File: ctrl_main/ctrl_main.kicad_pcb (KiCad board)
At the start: 2 copper layers, 53.3 x 101.6 mm, 18 parts, among them IC1 SN74HC125N, J1 B2B-XH-A(LF)(SN), J2 B2B-XH-A(LF)(SN), J3 B2B-XH-A(LF)(SN), P1 ANALOG, P2 DIGITAL_L, P3 DIGITAL_H, P4 JS_H, P5 JS_V, P6 SDC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

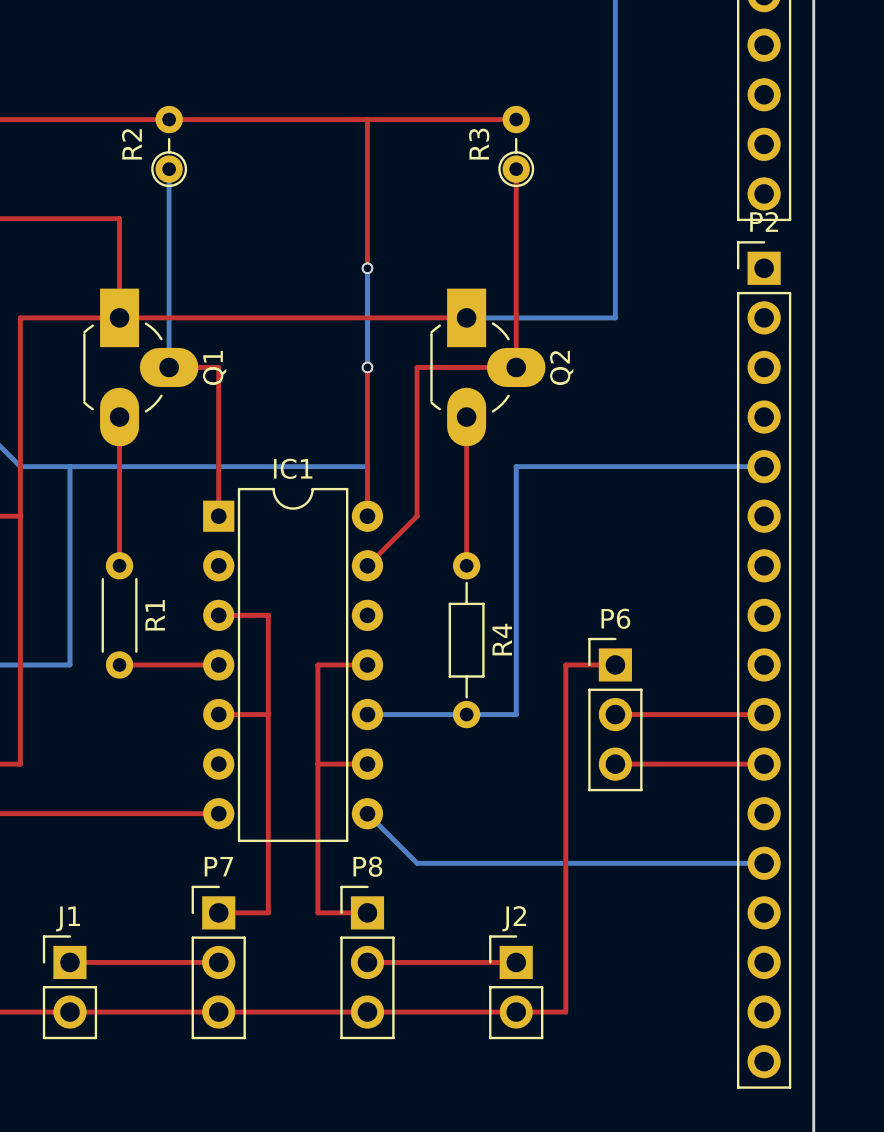
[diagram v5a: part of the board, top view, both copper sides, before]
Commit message: mod ctrl_main wiring
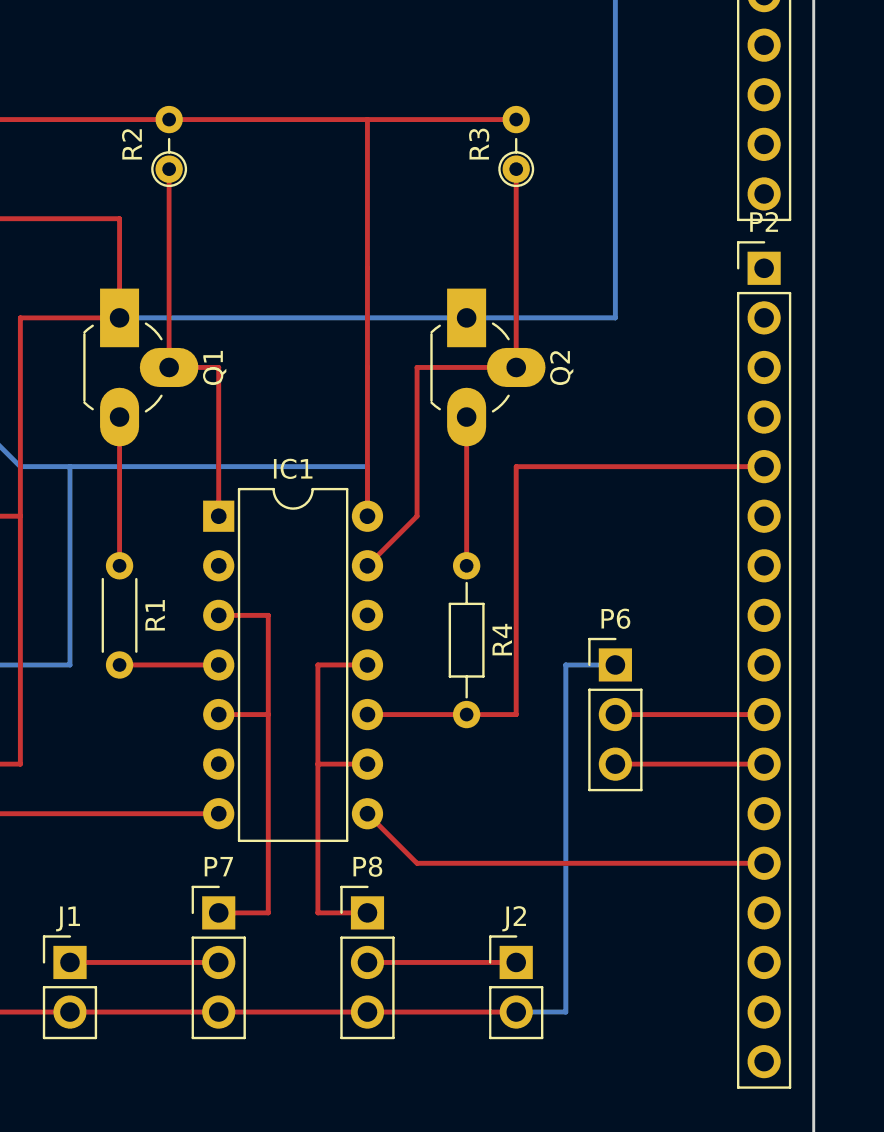
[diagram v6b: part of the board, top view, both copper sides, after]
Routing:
- net 5V: vias 2 -> 0
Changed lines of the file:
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@@
     (thickness 1.6)
     (drawings 23)
-    (tracks 81)
+    (tracks 79)
     (zones 0)
     (modules 18)
@@
   )
   (segment (start 214.63 124.46) (end 222.25 124.46) (width 0.25) (layer F.Cu) (net 1))
-  (segment (start 237.49 127) (end 240.03 127) (width 0.25) (layer F.Cu) (net 2))
-  (segment (start 240.03 109.22) (end 242.57 109.22) (width 0.25) (layer F.Cu) (net 2))
-  (segment (start 240.03 127) (end 240.03 109.22) (width 0.25) (layer F.Cu) (net 2))
+  (segment (start 217.17 91.44) (end 234.95 91.44) (width 0.25) (layer B.Cu) (net 2))
+  (segment (start 242.57 109.22) (end 240.03 109.22) (width 0.25) (layer B.Cu) (net 2))
+  (segment (start 240.03 127) (end 237.49 127) (width 0.25) (layer B.Cu) (net 2))
+  (segment (start 240.03 109.22) (end 240.03 127) (width 0.25) (layer B.Cu) (net 2))
   (segment (start 212.09 101.6) (end 212.09 91.44) (width 0.25) (layer F.Cu) (net 2))
   (segment (start 212.09 91.44) (end 217.17 91.44) (width 0.25) (layer F.Cu) (net 2))
@@
   (segment (start 212.09 101.6) (end 212.09 114.3) (width 0.25) (layer F.Cu) (net 2))
   (segment (start 234.95 91.44) (end 242.57 91.44) (width 0.25) (layer B.Cu) (net 2))
+  (segment (start 242.57 91.44) (end 242.57 71.12) (width 0.25) (layer B.Cu) (net 2))
+  (segment (start 242.57 71.12) (end 243.84 69.85) (width 0.25) (layer B.Cu) (net 2))
   (segment (start 243.84 69.85) (end 250.19 69.85) (width 0.25) (layer B.Cu) (net 2))
-  (segment (start 242.57 71.12) (end 243.84 69.85) (width 0.25) (layer B.Cu) (net 2))
-  (segment (start 242.57 91.44) (end 242.57 71.12) (width 0.25) (layer B.Cu) (net 2))
-  (segment (start 217.17 91.44) (end 234.95 91.44) (width 0.25) (layer F.Cu) (net 2))
   (segment (start 217.17 91.44) (end 217.17 86.36) (width 0.25) (layer F.Cu) (net 2))
   (segment (start 217.17 86.36) (end 209.55 86.36) (width 0.25) (layer F.Cu) (net 2))
@@
   (segment (start 201.93 86.36) (end 201.93 83.82) (width 0.25) (layer B.Cu) (net 2))
   (segment (start 229.87 124.46) (end 237.49 124.46) (width 0.25) (layer F.Cu) (net 3))
+  (segment (start 229.87 88.9) (end 229.87 93.98) (width 0.25) (layer F.Cu) (net 4))
+  (segment (start 229.87 81.28) (end 229.87 88.9) (width 0.25) (layer F.Cu) (net 4))
+  (segment (start 229.87 93.98) (end 229.87 101.6) (width 0.25) (layer F.Cu) (net 4))
   (segment (start 209.55 109.22) (end 214.63 109.22) (width 0.25) (layer B.Cu) (net 4))
   (segment (start 214.63 109.22) (end 214.63 99.06) (width 0.25) (layer B.Cu) (net 4))
-  (segment (start 229.87 101.6) (end 229.87 93.98) (width 0.25) (layer F.Cu) (net 4))
-  (segment (start 229.87 88.9) (end 229.87 81.28) (width 0.25) (layer F.Cu) (net 4))
-  (via (at 229.87 88.9) (size 0.6) (drill 0.4) (layers F.Cu B.Cu) (net 4))
-  (segment (start 229.87 93.98) (end 229.87 88.9) (width 0.25) (layer B.Cu) (net 4))
-  (via (at 229.87 93.98) (size 0.6) (drill 0.4) (layers F.Cu B.Cu) (net 4))
   (segment (start 229.87 101.6) (end 229.87 99.06) (width 0.25) (layer B.Cu) (net 4))
   (segment (start 212.09 99.06) (end 209.55 96.52) (width 0.25) (layer B.Cu) (net 4))
@@
   (segment (start 229.87 81.28) (end 237.49 81.28) (width 0.25) (layer F.Cu) (net 4))
   (segment (start 201.93 81.28) (end 219.71 81.28) (width 0.25) (layer F.Cu) (net 4))
-  (segment (start 219.71 83.82) (end 219.71 93.98) (width 0.25) (layer B.Cu) (net 5))
+  (segment (start 219.71 83.82) (end 219.71 93.98) (width 0.25) (layer F.Cu) (net 5))
   (segment (start 219.71 93.98) (end 222.25 93.98) (width 0.25) (layer F.Cu) (net 5))
   (segment (start 222.25 93.98) (end 222.25 101.6) (width 0.25) (layer F.Cu) (net 5))
@@
   (segment (start 217.17 104.14) (end 217.17 96.52) (width 0.25) (layer F.Cu) (net 9))
   (segment (start 234.95 104.14) (end 234.95 96.52) (width 0.25) (layer F.Cu) (net 10))
-  (segment (start 250.19 119.38) (end 232.41 119.38) (width 0.25) (layer B.Cu) (net 11))
-  (segment (start 232.41 119.38) (end 229.87 116.84) (width 0.25) (layer B.Cu) (net 11))
-  (segment (start 234.95 111.76) (end 237.49 111.76) (width 0.25) (layer B.Cu) (net 13) (status 10))
-  (segment (start 237.49 99.06) (end 250.19 99.06) (width 0.25) (layer B.Cu) (net 13))
-  (segment (start 237.49 111.76) (end 237.49 99.06) (width 0.25) (layer B.Cu) (net 13))
-  (segment (start 229.87 111.76) (end 234.95 111.76) (width 0.25) (layer B.Cu) (net 13) (status 20))
+  (segment (start 229.87 116.84) (end 232.41 119.38) (width 0.25) (layer F.Cu) (net 11))
+  (segment (start 232.41 119.38) (end 250.19 119.38) (width 0.25) (layer F.Cu) (net 11))
+  (segment (start 229.87 111.76) (end 234.95 111.76) (width 0.25) (layer F.Cu) (net 13))
+  (segment (start 250.19 99.06) (end 237.49 99.06) (width 0.25) (layer F.Cu) (net 13))
+  (segment (start 237.49 111.76) (end 234.95 111.76) (width 0.25) (layer F.Cu) (net 13))
+  (segment (start 237.49 99.06) (end 237.49 111.76) (width 0.25) (layer F.Cu) (net 13))
   (segment (start 222.25 109.22) (end 217.17 109.22) (width 0.25) (layer F.Cu) (net 14))
   (segment (start 201.93 88.9) (end 209.55 88.9) (width 0.25) (layer F.Cu) (net 19))
